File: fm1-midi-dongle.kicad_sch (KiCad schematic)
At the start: 30 parts, among them J1 TYPE-C 24P-GTJB 040, J2 TYPE-C-31-M-12, J3 PJ-320D, J4 PJ-320D, U1 CH32X035G8U6, U2 XC6206P332MR, U3 SY6280AAC, U4 H11L1SM

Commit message: PCB v3: priority-driven floorplan and full routing, DRC 0 / unconnected 0
- USB pair straight under the plug on F.Cu over the GND plane, no vias; DNP pull-downs removed (internal ones used)
- VBUS on the plug's back-face pads only, SY6280 2.5 mm away on the back; In2 = +3V3 plane; vias tented
- 10 mm jack pitch, receptacle on the right side, clamp keep-out both faces, numeric pad/hole spacing checks
- routed with the KAT router (kicad-pcb-autorouter-workflow skill), cfg in tools/cfg_fm1.py; post-route GND via
- Gerbers, Excellon, JLCPCB CPL + BOM, 3D renders, HTML layer viewer

Co-Authored-By: Claude Fable 5.1 <noreply@anthropic.com>
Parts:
- removed J1: TYPE-C 24P-GTJB 040, fm1_dongle:USB-C-SMD_TYPE-C-24P-GTJB-040, symbol fm1_dongle:USB-C_Plug_GTJB040
- removed R6: 15k, Resistor_SMD:R_0603_1608Metric, symbol Device:R
- C1, C2, C3: MPN (none) -> CL10A105KB8NNNC
- C4, C5: MPN (none) -> CC0603KRX7R9BB104
- D1: MPN (none) -> 1N4148W
- D2: MPN (none) -> 19-217/GHC-YR1S2/3T
- J1: renamed from R5; value 15k -> TYPE-C 24P-GTJB 040; footprint Resistor_SMD:R_0603_1608Metric -> fm1_dongle:USB-C-SMD_TYPE-C-24P-GTJB-040; symbol Device:R -> fm1_dongle:USB-C_Plug_GTJB040; LCSC# C22809 -> C3151751; MPN (none) -> TYPE-C 24P-GTJB 040; Note DNP: the X035 host port has internal pull-downs (RB_UH_PD_D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 -> SHOU HAN TYPE-C 24P-GTJB 040, board-edge clamp plug: PCB 0.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; now fitted
- J2: MPN (none) -> TYPE-C-31-M-12
- J3, J4: MPN (none) -> PJ-320D
- R1: MPN (none) -> 0603WAF5602T5E
- R10: MPN (none) -> 0603WAF1002T5E
- R11: MPN (none) -> 0603WAF1001T5E
- R12: MPN (none) -> 0603WAF1003T5E
- R2, R3: MPN (none) -> 0603WAF5101T5E
- R4: MPN (none) -> 0603WAF6801T5E
- R7: MPN (none) -> 0603WAF100JT5E
- R8: MPN (none) -> 0603WAF330JT5E
- R9: MPN (none) -> 0603WAF2200T5E
- U1: MPN (none) -> CH32X035G8U6
- U2: MPN (none) -> XC6206P332MR
- U3: MPN (none) -> SY6280AAC
- U4: MPN (none) -> H11L1SM
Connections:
- net CC_FM1: now also J1.A5 (CC1)
- net GND: now also J1.25 (GND), J1.26 (GND), J1.A1 (GND), J1.A12 (GND), J1.B1 (GND), J1.B12 (GND); no longer J1.2
- net USB_DM: now also J1.A7 (DN1); no longer J1.1
- net USB_DP: now also J1.A6 (DP1)
- net VBUS_FM1: now also J1.B4 (VBUS), J1.B9 (VBUS)
- no-connect marks 42 -> 44
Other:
- note added: "FM-1 MIDI dongle, rev A (netlist-first drawing: every connection is a net label; tidy before layout). JLCPCB build: PCB 0.8 mm (the plug clamps the board edge), all parts top side SMD, footprints from EasyEDA/LCSC. No D+/D- pull-downs: the X035 host port has them internally (RB_UH_PD_DIS = 0). TRS type A: tip = MIDI pin 5 (data), ring = pin 4 (source), sleeve = pin 2."
- note removed: "FM-1 MIDI dongle, rev A (netlist-first drawing: every connection is a net label; tidy before layout). JLCPCB build: PCB 0.8 mm (the plug clamps the board edge), all parts top side SMD, footprints from EasyEDA/LCSC. R5/R6 are DNP: the X035 host port has internal D+/D- pull-downs (RB_UH_PD_DIS = 0). TRS type A: tip = MIDI pin 5 (data), ring = pin 4 (source), sleeve = pin 2."

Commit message: PCB v4: single-sided placement, hand-written routing, silkscreen, rounded outline, case notches, 3D fixes
- gen_pcb.py: single-sided 20 x 37.7 mm floorplan, passives oriented toward their nets,
  convex corners rounded, two side locating notches (y 22.2, r 0.6) for a captured case,
  J2 3D offset fixed, KiCad-library models pointed at vendored STEP files
- route.py: explicit polylines (no autorouter), 45 deg bends only, no loops,
  0.2/0.3/0.5 mm tracks, 0.6/0.3 and 0.8/0.4 vias, GND planes and pours, +5V_IN pour
- silk.py: regenerated silkscreen (clipped outlines, pin-1/cathode marks, 0.8 mm
  designators, test-pad and back labels)
- check_loops.py, render_nets.py, render_route.py: review tools and renders in docs/
- house_rules.yaml + .kicad_dru: project rule override (USB plain 0.2 mm)
- plug WRL made opaque; R/C/LED 0603 and SOD-123 STEP vendored (KiCad 3D lib, CC-BY-SA 4.0)
- schematic: plug A9 NC (VBUS on A4/B4/B9)

DRC: 0 unconnected, 0 clearance errors; accepted items listed in DESIGN.md.

Co-Authored-By: Claude Opus 5.5 <noreply@anthropic.com>
Claude-Session: https://claude.ai/code/session_01Dtfv3zuhZTs975LiSXznFQ
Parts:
- J1: Note SHOU HAN TYPE-C 24P-GTJB 040, board-edge clamp plug: PCB 0.80 +/-0.05 mm, pads on both faces (datasheet p.2); JLCPCB Standard assembly only. VBUS taken on the back-face pads B4/B9 only (A4/A9 joined inside the plug; no via fits under the clamp) -> SHOU HAN TYPE-C 24P-GTJB 040, board-edge clamp plug: PCB 0.80 +/-0.05 mm, pads on both faces (datasheet p.2); JLCPCB Standard assembly only. VBUS on A4 (top) + B4/B9 (back, joined to A4 by a via): 3 of 4 contacts, ~0.33 A each at the 1 A limit. A9 is NC: it sits right of the USB pair and the DIO/RX traces pass under it
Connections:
- net VBUS_FM1: now also J1.A4 (VBUS)
- no-connect marks 44 -> 43
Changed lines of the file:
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@@
 		(property "LCSC#" "C3151751" (at 279.4 90.17 0) (effects (font (size 1.27 1.27)) (justify left) (hide yes)))
 		(property "MPN" "TYPE-C 24P-GTJB 040" (at 279.4 90.17 0) (effects (font (size 1.27 1.27)) (justify left) (hide yes)))
-		(property "Note" "SHOU HAN TYPE-C 24P-GTJB 040, board-edge clamp plug: PCB 0.80 +/-0.05 mm, pads on both faces (datasheet p.2); JLCPCB Standard assembly only. VBUS taken on the back-face pads B4/B9 only (A4/A9 joined inside the plug; no via fits under the clamp)" (at 279.4 90.17 0) (effects (font (size 1.27 1.27)) (justify left) (hide yes)))
+		(property "Note" "SHOU HAN TYPE-C 24P-GTJB 040, board-edge clamp plug: PCB 0.80 +/-0.05 mm, pads on both faces (datasheet p.2); JLCPCB Standard assembly only. VBUS on A4 (top) + B4/B9 (back, joined to A4 by a via): 3 of 4 contacts, ~0.33 A each at the 1 A limit. A9 is NC: it sits right of the USB pair and the DIO/RX traces pass under it" (at 279.4 90.17 0) (effects (font (size 1.27 1.27)) (justify left) (hide yes)))
 		(pin "A12")
 		(pin "A11")
@@
 	(wire (pts (xy 265.43 93.98) (xy 262.89 93.98)) (stroke (width 0) (type default)))
 	(label "CC_FM1" (at 262.89 93.98 180) (effects (font (size 1.27 1.27)) (justify right bottom)))
-	(no_connect (at 265.43 96.52))
+	(wire (pts (xy 265.43 96.52) (xy 262.89 96.52)) (stroke (width 0) (type default)))
+	(label "VBUS_FM1" (at 262.89 96.52 180) (effects (font (size 1.27 1.27)) (justify right bottom)))
 	(no_connect (at 265.43 99.06))
 	(no_connect (at 265.43 101.6))

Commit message: D2 to Basic red LED C2286 (green C72043 out of stock); add 3D views
- gen_sch.py / BOM.csv: D2 KT-0603R (C2286, Basic): no Extended fee, ~1.3 mA via R11 1k
- schematic and board regenerated: ERC 0, DRC unchanged (accepted items only)
- docs/views: top, bottom, isometric front/back/under, side and front renders

Co-Authored-By: Claude Opus 5.5 <noreply@anthropic.com>
Claude-Session: https://claude.ai/code/session_01Dtfv3zuhZTs975LiSXznFQ
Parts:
- D2: value LED green 0603 -> LED red 0603; LCSC# C72043 -> C2286; MPN 19-217/GHC-YR1S2/3T -> KT-0603R
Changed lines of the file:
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@@
 	(symbol (lib_id "Device:LED") (at 265.43 160.02 0) (unit 1) (exclude_from_sim no) (in_bom yes) (on_board yes) (dnp no)
 		(property "Reference" "D2" (at 267.97 157.48 0) (effects (font (size 1.27 1.27)) (justify left)))
-		(property "Value" "LED green 0603" (at 267.97 160.02 0) (effects (font (size 1.27 1.27)) (justify left)))
+		(property "Value" "LED red 0603" (at 267.97 160.02 0) (effects (font (size 1.27 1.27)) (justify left)))
 		(property "Footprint" "LED_SMD:LED_0603_1608Metric" (at 265.43 160.02 0) (effects (font (size 1.27 1.27)) (justify left) (hide yes)))
 		(property "Datasheet" "~" (at 265.43 160.02 0) (effects (font (size 1.27 1.27)) (justify left) (hide yes)))
-		(property "LCSC#" "C72043" (at 265.43 160.02 0) (effects (font (size 1.27 1.27)) (justify left) (hide yes)))
-		(property "MPN" "19-217/GHC-YR1S2/3T" (at 265.43 160.02 0) (effects (font (size 1.27 1.27)) (justify left) (hide yes)))
+		(property "LCSC#" "C2286" (at 265.43 160.02 0) (effects (font (size 1.27 1.27)) (justify left) (hide yes)))
+		(property "MPN" "KT-0603R" (at 265.43 160.02 0) (effects (font (size 1.27 1.27)) (justify left) (hide yes)))
 		(pin "1")
 		(pin "2")

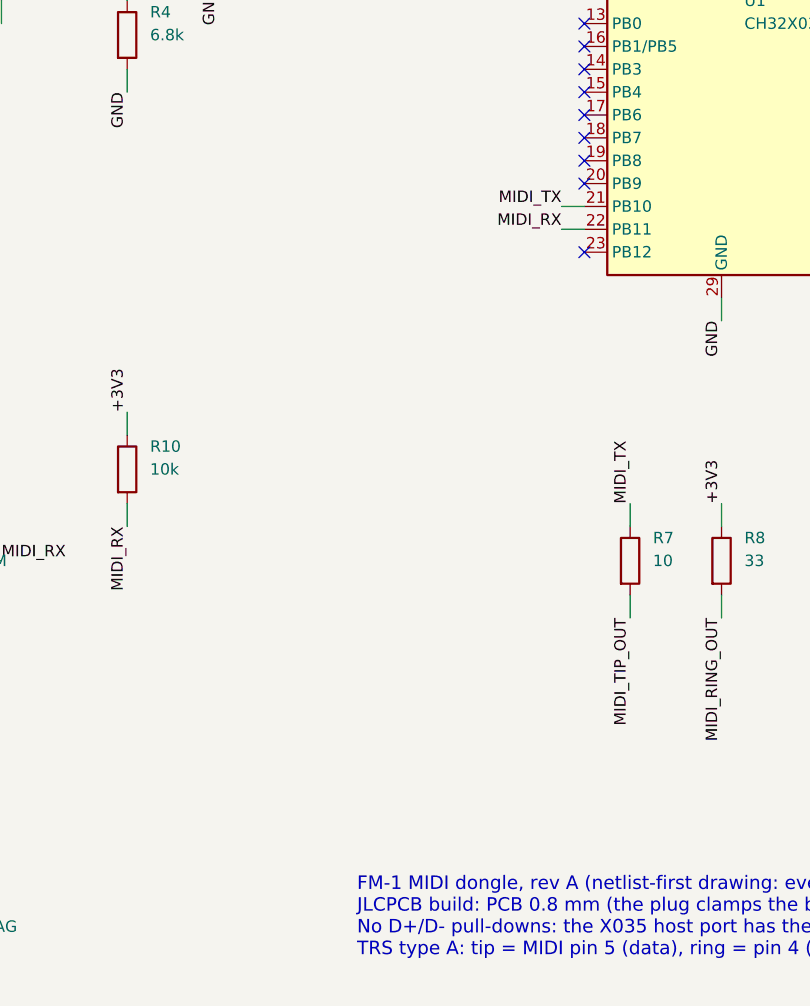
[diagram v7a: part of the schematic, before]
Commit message: Add hardware MIDI THRU: U5 SPDT switch selects OUT jack source
SN74LVC1G3157DCKR (LCSC C38663) in front of R7/J3 tip: S low = MIDI_RX
(opto output, hardware THRU), S high = MIDI_TX. S = OUT_SEL = PB9 with
R13 100k pull-down so THRU is the default with a blank or resetting MCU.

Layout: U5 between MCU and opto, C5 and R13 moved, TP3 (GND) moved to
the pocket above the jacks. ERC 0, DRC only the 6 known J1 edge items.
BOM, DESIGN.md and renders updated; SC-70-6 STEP vendored.

Co-Authored-By: Claude Opus 5.5 <noreply@anthropic.com>
Claude-Session: https://claude.ai/code/session_01Dtfv3zuhZTs975LiSXznFQ
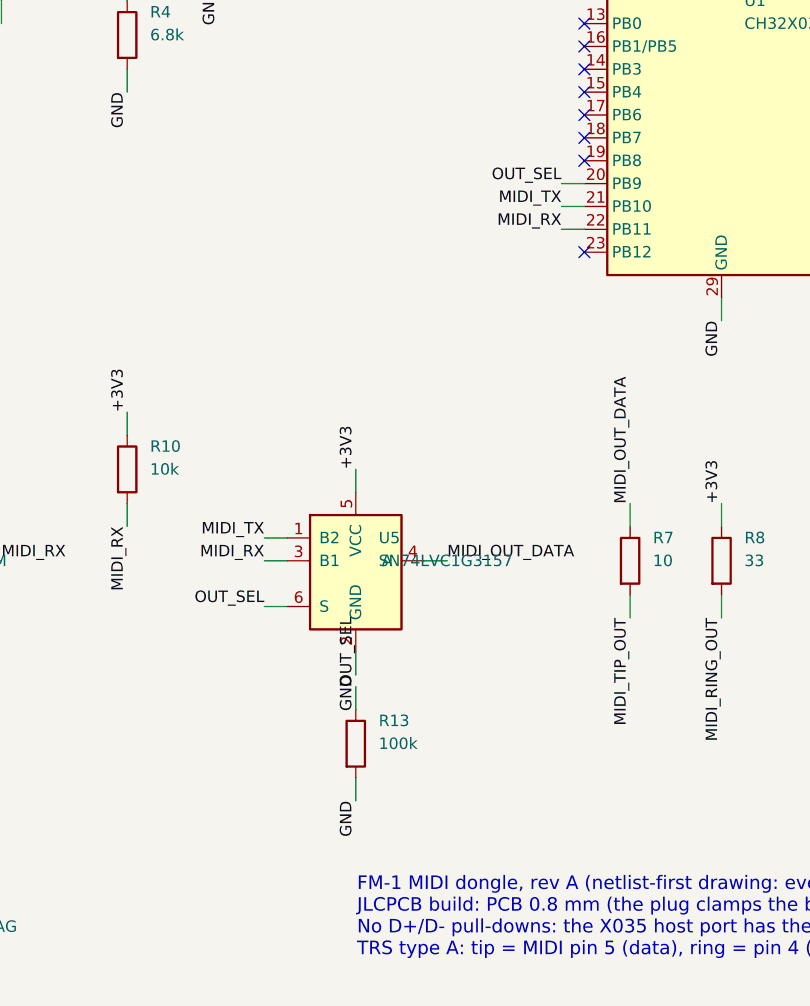
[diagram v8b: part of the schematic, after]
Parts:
- removed R7: 10, Resistor_SMD:R_0603_1608Metric, symbol Device:R
- added J4: PJ-320D, fm1_dongle:AUDIO-SMD_PJ-320D, symbol fm1_dongle:PJ-320D
- added R13: 100k, Resistor_SMD:R_0603_1608Metric, symbol Device:R
- added U5: SN74LVC1G3157, Package_TO_SOT_SMD:SOT-363_SC-70-6, symbol fm1_dongle:SN74LVC1G3157
- R7: renamed from J4; value PJ-320D -> 10; footprint fm1_dongle:AUDIO-SMD_PJ-320D -> Resistor_SMD:R_0603_1608Metric; symbol fm1_dongle:PJ-320D -> Device:R; LCSC# C521460 -> C22859; MPN PJ-320D -> 0603WAF100JT5E; Note sleeve (1, 2) left open at the receiver (MIDI spec). tip=4,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 -> (none)
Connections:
- net +3V3: now also U5.5 (VCC)
- net GND: now also R13.2, U5.2 (GND)
- net MIDI_IN_RING: now also J4.3; no longer R7.3
- net MIDI_IN_TIP: now also J4.4; no longer R7.4
- net MIDI_RX: now also U5.3 (B1)
- net MIDI_TIP_OUT: now also R7.2
- net MIDI_TX: now also U5.1 (B2)
- net OUT_SEL: now reaches U1.20 (PB9)
- net OUT_SEL: now also R13.1, U5.6 (S)
- net MIDI_OUT_DATA: now reaches R7.1
- net MIDI_OUT_DATA: now also U5.4 (A)
- no-connect marks 43 -> 42
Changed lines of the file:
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@@
 	(no_connect (at 175.26 102.87))
 	(no_connect (at 175.26 105.41))
-	(no_connect (at 175.26 107.95))
+	(wire (pts (xy 175.26 107.95) (xy 172.72 107.95)) (stroke (width 0) (type default)))
+	(label "OUT_SEL" (at 172.72 107.95 180) (effects (font (size 1.27 1.27)) (justify right bottom)))
 	(wire (pts (xy 175.26 110.49) (xy 172.72 110.49)) (stroke (width 0) (type default)))
 	(label "MIDI_TX" (at 172.72 110.49 180) (effects (font (size 1.27 1.27)) (justify right bottom)))
@@
 	(wire (pts (xy 309.88 63.5) (xy 309.88 66.04)) (stroke (width 0) (type default)))
 	(label "CC_FM1" (at 309.88 66.04 270) (effects (font (size 1.27 1.27)) (justify right bottom)))
+	(symbol (lib_id "fm1_dongle:SN74LVC1G3157") (at 149.86 149.86 0) (unit 1) (exclude_from_sim no) (in_bom yes) (on_board yes) (dnp no)
+		(property "Reference" "U5" (at 152.4 147.32 0) (effects (font (size 1.27 1.27)) (justify left)))
+		(property "Value" "SN74LVC1G3157" (at 152.4 149.86 0) (effects (font (size 1.27 1.27)) (justify left)))
+		(property "Footprint" "Package_TO_SOT_SMD:SOT-363_SC-70-6" (at 149.86 149.86 0) (effects (font (size 1.27 1.27)) (justify left) (hide yes)))
+		(property "Datasheet" "~" (at 149.86 149.86 0) (effects (font (size 1.27 1.27)) (justify left) (hide yes)))
+		(property "LCSC#" "C38663" (at 149.86 149.86 0) (effects (font (size 1.27 1.27)) (justify left) (hide yes)))
+		(property "MPN" "SN74LVC1G3157DCKR" (at 149.86 149.86 0) (effects (font (size 1.27 1.27)) (justify left) (hide yes)))
+		(property "Note" "TI SCES424O: 1 B2, 2 GND, 3 B1, 4 A, 5 VCC, 6 S; S low A=B1, S high A=B2. Ron <= 25 ohm at 3 V" (at 149.86 149.86 0) (effects (font (size 1.27 1.27)) (justify left) (hide yes)))
+		(pin "1")
+		(pin "2")
+		(pin "3")
+		(pin "4")
+		(pin "5")
+		(pin "6")
+		(instances (project "fm1-midi-dongle" (path "/7f2a1c4e-0b3d-4c1a-9e8f-5a6b7c8d9e0f" (reference "U5") (unit 1))))
+	)
+	(wire (pts (xy 142.24 147.32) (xy 139.7 147.32)) (stroke (width 0) (type default)))
+	(label "MIDI_TX" (at 139.7 147.32 180) (effects (font (size 1.27 1.27)) (justify right bottom)))
+	(wire (pts (xy 149.86 160.02) (xy 149.86 162.56)) (stroke (width 0) (type default)))
+	(label "GND" (at 149.86 162.56 270) (effects (font (size 1.27 1.27)) (justify right bottom)))
+	(wire (pts (xy 142.24 149.86) (xy 139.7 149.86)) (stroke (width 0) (type default)))
+	(label "MIDI_RX" (at 139.7 149.86 180) (effects (font (size 1.27 1.27)) (justify right bottom)))
+	(wire (pts (xy 157.48 149.86) (xy 160.02 149.86)) (stroke (width 0) (type default)))
+	(label "MIDI_OUT_DATA" (at 160.02 149.86 0) (effects (font (size 1.27 1.27)) (justify left bottom)))
+	(wire (pts (xy 149.86 142.24) (xy 149.86 139.7)) (stroke (width 0) (type default)))
+	(label "+3V3" (at 149.86 139.7 90) (effects (font (size 1.27 1.27)) (justify left bottom)))
+	(wire (pts (xy 142.24 154.94) (xy 139.7 154.94)) (stroke (width 0) (type default)))
+	(label "OUT_SEL" (at 139.7 154.94 180) (effects (font (size 1.27 1.27)) (justify right bottom)))
+	(symbol (lib_id "Device:R") (at 149.86 170.18 0) (unit 1) (exclude_from_sim no) (in_bom yes) (on_board yes) (dnp no)
+		(property "Reference" "R13" (at 152.4 167.64 0) (effects (font (size 1.27 1.27)) (justify left)))
+		(property "Value" "100k" (at 152.4 170.18 0) (effects (font (size 1.27 1.27)) (justify left)))
+		(property "Footprint" "Resistor_SMD:R_0603_1608Metric" (at 149.86 170.18 0) (effects (font (size 1.27 1.27)) (justify left) (hide yes)))
+		(property "Datasheet" "~" (at 149.86 170.18 0) (effects (font (size 1.27 1.27)) (justify left) (hide yes)))
+		(property "LCSC#" "C25803" (at 149.86 170.18 0) (effects (font (size 1.27 1.27)) (justify left) (hide yes)))
+		(property "MPN" "0603WAF1003T5E" (at 149.86 170.18 0) (effects (font (size 1.27 1.27)) (justify left) (hide yes)))
+		(property "Note" "OUT_SEL default low = hardware THRU until firmware drives PB9 high" (at 149.86 170.18 0) (effects (font (size 1.27 1.27)) (justify left) (hide yes)))
+		(pin "1")
+		(pin "2")
+		(instances (project "fm1-midi-dongle" (path "/7f2a1c4e-0b3d-4c1a-9e8f-5a6b7c8d9e0f" (reference "R13") (unit 1))))
+	)
+	(wire (pts (xy 149.86 166.37) (xy 149.86 163.83)) (stroke (width 0) (type default)))
+	(label "OUT_SEL" (at 149.86 163.83 90) (effects (font (size 1.27 1.27)) (justify left bottom)))
+	(wire (pts (xy 149.86 173.99) (xy 149.86 176.53)) (stroke (width 0) (type default)))
+	(label "GND" (at 149.86 176.53 270) (effects (font (size 1.27 1.27)) (justify right bottom)))
 	(symbol (lib_id "Device:R") (at 180.34 149.86 0) (unit 1) (exclude_from_sim no) (in_bom yes) (on_board yes) (dnp no)
 		(property "Reference" "R7" (at 182.88 147.32 0) (effects (font (size 1.27 1.27)) (justify left)))
@@
 	)
 	(wire (pts (xy 180.34 146.05) (xy 180.34 143.51)) (stroke (width 0) (type default)))
-	(label "MIDI_TX" (at 180.34 143.51 90) (effects (font (size 1.27 1.27)) (justify left bottom)))
+	(label "MIDI_OUT_DATA" (at 180.34 143.51 90) (effects (font (size 1.27 1.27)) (justify left bottom)))
 	(wire (pts (xy 180.34 153.67) (xy 180.34 156.21)) (stroke (width 0) (type default)))
 	(label "MIDI_TIP_OUT" (at 180.34 156.21 270) (effects (font (size 1.27 1.27)) (justify right bottom)))
